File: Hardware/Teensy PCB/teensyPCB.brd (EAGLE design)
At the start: 100 x 50 mm, 0 parts

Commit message: added some parts
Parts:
- added J_BT_BOARD_1: BLUETOOTH_BOARD, Bluetooth_HC-05:BT_BOARD_FOOTPRINT
- added J_ULTRASONIC_1: HC-SR04, HC-SR04:HC-SR04_FOOTPRINT
- added U$1: TEENSY_3.1_ALL_PINS_AND_PADS, Teensy_3_and_LC_Series_Boards_v1.1:TEENSY3_ALL_PINS_&_PADS
- added U1: HC_05, Bluetooth_HC-05:BLUETOOTH_SMD
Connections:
- new net 3.3V: U$1.3.3V, U$1.3.3V1, U$1.3.3V2
- new net AGND: U$1.AGND
- new net AREF: U$1.AREF
- new net GND: U$1.GND, U$1.GND1, U$1.GND2
- new net VBAT: U$1.VBAT
- new net VIN: U$1.VIN
- new net VUSB: U$1.VUSB
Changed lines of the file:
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@@
 <setting verticaltext="up"/>
 </settings>
-<grid distance="50" unitdist="mm" unit="mm" style="lines" multiple="1" display="yes" altdistance="0.025" altunitdist="inch" altunit="inch"/>
+<grid distance="5" unitdist="mm" unit="mm" style="lines" multiple="1" display="yes" altdistance="0.025" altunitdist="inch" altunit="inch"/>
 <layers>
 <layer number="1" name="Top" color="4" fill="1" visible="yes" active="yes"/>
@@
 <layer number="48" name="Document" color="7" fill="1" visible="yes" active="yes"/>
 <layer number="49" name="Reference" color="7" fill="1" visible="yes" active="yes"/>
+<layer number="50" name="dxf" color="7" fill="1" visible="yes" active="yes"/>
 <layer number="51" name="tDocu" color="7" fill="1" visible="yes" active="yes"/>
 <layer number="52" name="bDocu" color="7" fill="1" visible="yes" active="yes"/>
+<layer number="53" name="tGND_GNDA" color="7" fill="9" visible="no" active="no"/>
+<layer number="54" name="bGND_GNDA" color="1" fill="9" visible="no" active="no"/>
+<layer number="56" name="wert" color="7" fill="1" visible="yes" active="yes"/>
 <layer number="90" name="Modules" color="5" fill="1" visible="no" active="no"/>
 <layer number="91" name="Nets" color="2" fill="1" visible="no" active="no"/>
@@
 <layer number="97" name="Info" color="7" fill="1" visible="no" active="no"/>
 <layer number="98" name="Guide" color="6" fill="1" visible="no" active="no"/>
+<layer number="100" name="Muster" color="7" fill="1" visible="no" active="no"/>
+<layer number="101" name="Patch_Top" color="12" fill="4" visible="yes" active="yes"/>
+<layer number="102" name="Vscore" color="7" fill="1" visible="yes" active="yes"/>
+<layer number="104" name="Name" color="7" fill="1" visible="yes" active="yes"/>
+<layer number="116" name="Patch_BOT" color="9" fill="4" visible="yes" active="yes"/>
+<layer number="121" name="_tsilk" color="7" fill="1" visible="yes" active="yes"/>
+<layer number="122" name="_bsilk" color="7" fill="1" visible="yes" active="yes"/>
+<layer number="151" name="HeatSink" color="7" fill="1" visible="yes" active="yes"/>
+<layer number="200" name="200bmp" color="1" fill="10" visible="no" active="no"/>
+<layer number="201" name="201bmp" color="2" fill="1" visible="no" active="no"/>
+<layer number="202" name="202bmp" color="3" fill="1" visible="no" active="no"/>
+<layer number="250" name="Descript" color="3" fill="1" visible="no" active="no"/>
+<layer number="251" name="SMDround" color="12" fill="11" visible="no" active="no"/>
+<layer number="254" name="cooling" color="7" fill="1" visible="yes" active="yes"/>
 </layers>
 <board>
@@
 </autorouter>
 <elements>
+<element name="U$1" library="Teensy_3_and_LC_Series_Boards_v1.1" package="TEENSY3_ALL_PINS_&amp;_PADS" value="TEENSY_3.1_ALL_PINS_AND_PADS" x="-50" y="50"/>
+<element name="U1" library="Bluetooth_HC-05" package="BLUETOOTH_SMD" value="HC_05" x="-100" y="50"/>
+<element name="J_BT_BOARD_1" library="Bluetooth_HC-05" package="BT_BOARD_FOOTPRINT" value="BLUETOOTH_BOARD" x="-30" y="-25"/>
+<element name="J_ULTRASONIC_1" library="HC-SR04" package="HC-SR04_FOOTPRINT" value="HC-SR04" x="-75" y="-25"/>
 </elements>
 <signals>
+<signal name="GND">
+<contactref element="U$1" pad="GND1"/>
+<contactref element="U$1" pad="GND"/>
+<contactref element="U$1" pad="GND2"/>
+<wire x1="-50" y1="48.73" x2="-50" y2="33.49" width="0" layer="19" extent="1-1"/>
+<wire x1="-57.62" y1="66.51" x2="-50" y2="48.73" width="0" layer="19" extent="1-1"/>
+</signal>
+<signal name="VIN">
+<contactref element="U$1" pad="VIN"/>
+</signal>
+<signal name="AGND">
+<contactref element="U$1" pad="AGND"/>
+</signal>
+<signal name="3.3V">
+<contactref element="U$1" pad="3.3V2"/>
+<contactref element="U$1" pad="3.3V1"/>
+<contactref element="U$1" pad="3.3V"/>
+<wire x1="-47.46" y1="48.73" x2="-42.38" y2="61.43" width="0" layer="19" extent="1-1"/>
+<wire x1="-52.54" y1="33.49" x2="-47.46" y2="48.73" width="0" layer="19" extent="1-1"/>
+</signal>
+<signal name="VBAT">
+<contactref element="U$1" pad="VBAT"/>
+</signal>
+<signal name="AREF">
+<contactref element="U$1" pad="AREF"/>
+</signal>
+<signal name="VUSB">
+<contactref element="U$1" pad="VUSB"/>
+</signal>
 </signals>
 </board>

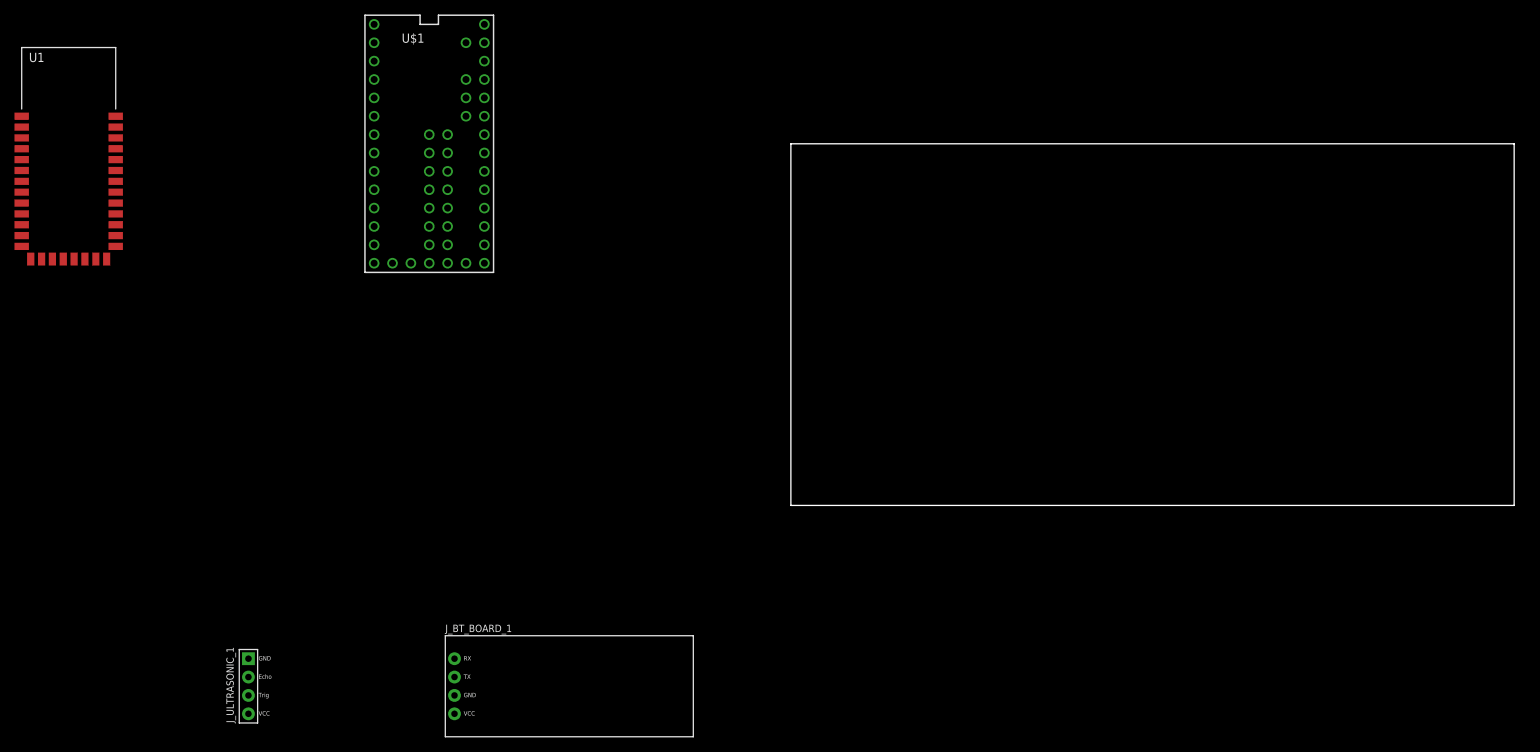
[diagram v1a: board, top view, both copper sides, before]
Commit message: reserving audio pins
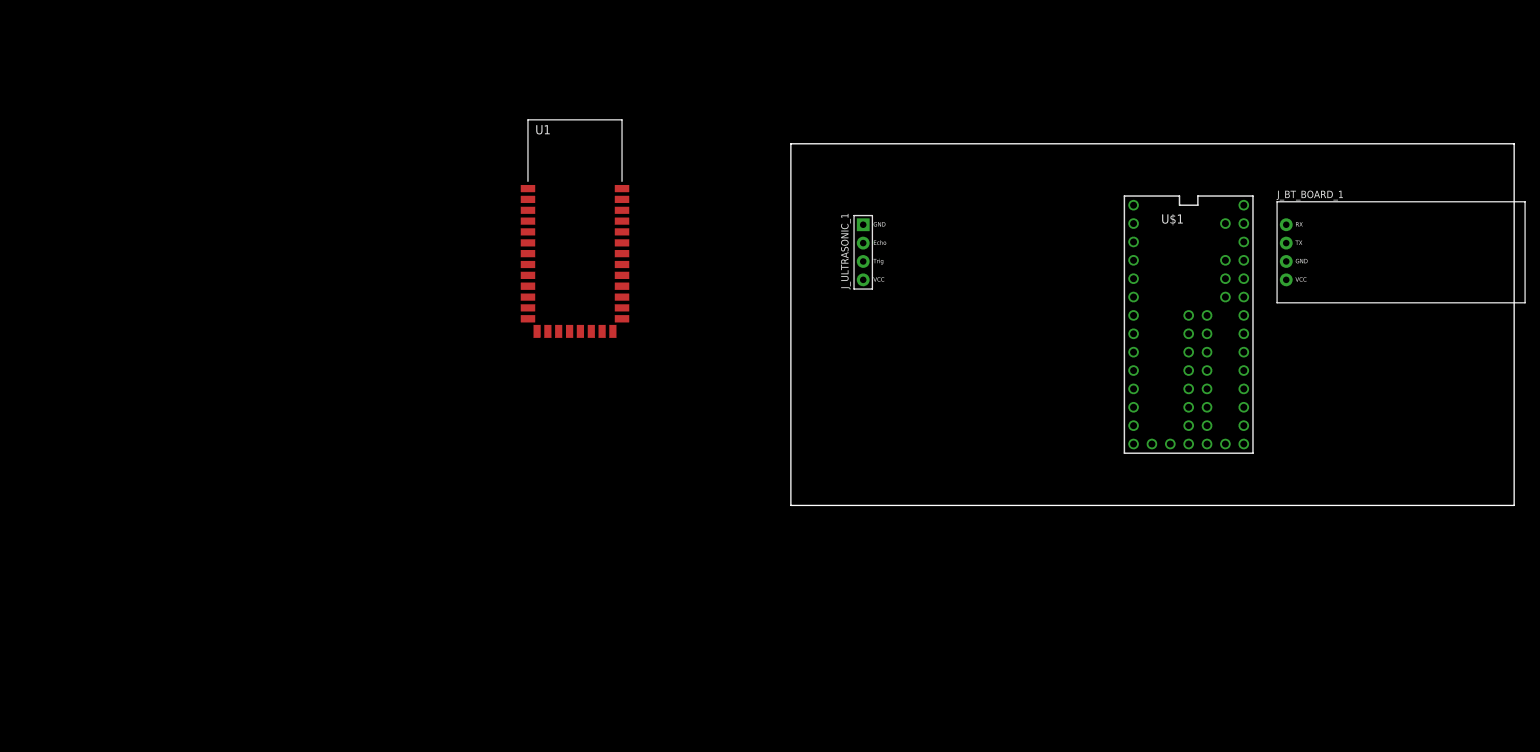
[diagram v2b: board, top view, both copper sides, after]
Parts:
- moved J_BT_BOARD_1 129.7 mm to (85.0, 35.0)
- moved U$1 107.9 mm to (55.0, 25.0)
- moved J_ULTRASONIC_1 104.0 mm to (10.0, 35.0)
- moved U1 70.7 mm to (-30.0, 40.0)
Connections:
- net GND: now also U$1.10, U$1.11, U$1.12, U$1.13, U$1.14/A0, U$1.15/A1, U$1.18/A4, U$1.19/A5, U$1.22/A8, U$1.23/A9, U$1.7, U$1.9
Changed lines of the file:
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@@
 <layer number="101" name="Patch_Top" color="12" fill="4" visible="yes" active="yes"/>
 <layer number="102" name="Vscore" color="7" fill="1" visible="yes" active="yes"/>
+<layer number="103" name="tMap" color="7" fill="1" visible="yes" active="yes"/>
 <layer number="104" name="Name" color="7" fill="1" visible="yes" active="yes"/>
+<layer number="105" name="tPlate" color="7" fill="1" visible="yes" active="yes"/>
+<layer number="106" name="bPlate" color="7" fill="1" visible="yes" active="yes"/>
+<layer number="107" name="Crop" color="7" fill="1" visible="yes" active="yes"/>
+<layer number="108" name="tplace-old" color="10" fill="1" visible="no" active="yes"/>
+<layer number="109" name="ref-old" color="11" fill="1" visible="no" active="yes"/>
 <layer number="116" name="Patch_BOT" color="9" fill="4" visible="yes" active="yes"/>
 <layer number="121" name="_tsilk" color="7" fill="1" visible="yes" active="yes"/>
 <layer number="122" name="_bsilk" color="7" fill="1" visible="yes" active="yes"/>
+<layer number="125" name="_tNames" color="7" fill="1" visible="yes" active="yes"/>
+<layer number="144" name="Drill_legend" color="7" fill="1" visible="yes" active="yes"/>
 <layer number="151" name="HeatSink" color="7" fill="1" visible="yes" active="yes"/>
+<layer number="199" name="Contour" color="7" fill="1" visible="yes" active="yes"/>
 <layer number="200" name="200bmp" color="1" fill="10" visible="no" active="no"/>
 <layer number="201" name="201bmp" color="2" fill="1" visible="no" active="no"/>
 <layer number="202" name="202bmp" color="3" fill="1" visible="no" active="no"/>
+<layer number="203" name="203bmp" color="4" fill="10" visible="yes" active="yes"/>
+<layer number="204" name="204bmp" color="5" fill="10" visible="yes" active="yes"/>
+<layer number="205" name="205bmp" color="6" fill="10" visible="yes" active="yes"/>
+<layer number="206" name="206bmp" color="7" fill="10" visible="yes" active="yes"/>
+<layer number="207" name="207bmp" color="8" fill="10" visible="yes" active="yes"/>
+<layer number="208" name="208bmp" color="9" fill="10" visible="yes" active="yes"/>
+<layer number="209" name="209bmp" color="7" fill="1" visible="yes" active="yes"/>
+<layer number="210" name="210bmp" color="7" fill="1" visible="yes" active="yes"/>
+<layer number="211" name="211bmp" color="7" fill="1" visible="yes" active="yes"/>
+<layer number="212" name="212bmp" color="7" fill="1" visible="yes" active="yes"/>
+<layer number="213" name="213bmp" color="7" fill="1" visible="yes" active="yes"/>
+<layer number="214" name="214bmp" color="7" fill="1" visible="yes" active="yes"/>
+<layer number="215" name="215bmp" color="7" fill="1" visible="yes" active="yes"/>
+<layer number="216" name="216bmp" color="7" fill="1" visible="yes" active="yes"/>
+<layer number="217" name="217bmp" color="18" fill="1" visible="no" active="no"/>
+<layer number="218" name="218bmp" color="19" fill="1" visible="no" active="no"/>
+<layer number="219" name="219bmp" color="20" fill="1" visible="no" active="no"/>
+<layer number="220" name="220bmp" color="21" fill="1" visible="no" active="no"/>
+<layer number="221" name="221bmp" color="22" fill="1" visible="no" active="no"/>
+<layer number="222" name="222bmp" color="23" fill="1" visible="no" active="no"/>
+<layer number="223" name="223bmp" color="24" fill="1" visible="no" active="no"/>
+<layer number="224" name="224bmp" color="25" fill="1" visible="no" active="no"/>
 <layer number="250" name="Descript" color="3" fill="1" visible="no" active="no"/>
 <layer number="251" name="SMDround" color="12" fill="11" visible="no" active="no"/>
@@
 </autorouter>
 <elements>
-<element name="U$1" library="Teensy_3_and_LC_Series_Boards_v1.1" package="TEENSY3_ALL_PINS_&amp;_PADS" value="TEENSY_3.1_ALL_PINS_AND_PADS" x="-50" y="50"/>
-<element name="U1" library="Bluetooth_HC-05" package="BLUETOOTH_SMD" value="HC_05" x="-100" y="50"/>
-<element name="J_BT_BOARD_1" library="Bluetooth_HC-05" package="BT_BOARD_FOOTPRINT" value="BLUETOOTH_BOARD" x="-30" y="-25"/>
-<element name="J_ULTRASONIC_1" library="HC-SR04" package="HC-SR04_FOOTPRINT" value="HC-SR04" x="-75" y="-25"/>
+<element name="U$1" library="Teensy_3_and_LC_Series_Boards_v1.1" package="TEENSY3_ALL_PINS_&amp;_PADS" value="TEENSY_3.1_ALL_PINS_AND_PADS" x="55" y="25"/>
+<element name="U1" library="Bluetooth_HC-05" package="BLUETOOTH_SMD" value="HC_05" x="-30" y="40"/>
+<element name="J_BT_BOARD_1" library="Bluetooth_HC-05" package="BT_BOARD_FOOTPRINT" value="BLUETOOTH_BOARD" x="85" y="35"/>
+<element name="J_ULTRASONIC_1" library="HC-SR04" package="HC-SR04_FOOTPRINT" value="HC-SR04" x="10" y="35"/>
 </elements>
 <signals>
@@
 <contactref element="U$1" pad="GND"/>
 <contactref element="U$1" pad="GND2"/>
-<wire x1="-50" y1="48.73" x2="-50" y2="33.49" width="0" layer="19" extent="1-1"/>
-<wire x1="-57.62" y1="66.51" x2="-50" y2="48.73" width="0" layer="19" extent="1-1"/>
+<contactref element="U$1" pad="18/A4"/>
+<contactref element="U$1" pad="19/A5"/>
+<contactref element="U$1" pad="11"/>
+<contactref element="U$1" pad="9"/>
+<contactref element="U$1" pad="23/A9"/>
+<contactref element="U$1" pad="22/A8"/>
+<contactref element="U$1" pad="13"/>
+<contactref element="U$1" pad="15/A1"/>
+<contactref element="U$1" pad="12"/>
+<contactref element="U$1" pad="14/A0"/>
+<contactref element="U$1" pad="7"/>
+<contactref element="U$1" pad="10"/>
+<wire x1="62.62" y1="31.35" x2="62.62" y2="33.89" width="0" layer="19" extent="1-1"/>
+<wire x1="62.62" y1="23.73" x2="62.62" y2="31.35" width="0" layer="19" extent="1-1"/>
+<wire x1="62.62" y1="21.19" x2="62.62" y2="23.73" width="0" layer="19" extent="1-1"/>
+<wire x1="55" y1="23.73" x2="62.62" y2="23.73" width="0" layer="19" extent="1-1"/>
+<wire x1="62.62" y1="13.57" x2="62.62" y2="21.19" width="0" layer="19" extent="1-1"/>
+<wire x1="62.62" y1="11.03" x2="62.62" y2="13.57" width="0" layer="19" extent="1-1"/>
+<wire x1="62.62" y1="8.49" x2="62.62" y2="11.03" width="0" layer="19" extent="1-1"/>
+<wire x1="55" y1="8.49" x2="62.62" y2="8.49" width="0" layer="19" extent="1-1"/>
+<wire x1="47.38" y1="8.49" x2="55" y2="8.49" width="0" layer="19" extent="1-1"/>
+<wire x1="47.38" y1="11.03" x2="47.38" y2="8.49" width="0" layer="19" extent="1-1"/>
+<wire x1="47.38" y1="13.57" x2="47.38" y2="11.03" width="0" layer="19" extent="1-1"/>
+<wire x1="47.38" y1="16.11" x2="47.38" y2="13.57" width="0" layer="19" extent="1-1"/>
+<wire x1="47.38" y1="21.19" x2="47.38" y2="16.11" width="0" layer="19" extent="1-1"/>
+<wire x1="47.38" y1="41.51" x2="62.62" y2="33.89" width="0" layer="19" extent="1-1"/>
 </signal>
 <signal name="VIN">
@@
 <contactref element="U$1" pad="3.3V1"/>
 <contactref element="U$1" pad="3.3V"/>
-<wire x1="-47.46" y1="48.73" x2="-42.38" y2="61.43" width="0" layer="19" extent="1-1"/>
-<wire x1="-52.54" y1="33.49" x2="-47.46" y2="48.73" width="0" layer="19" extent="1-1"/>
+<wire x1="57.54" y1="23.73" x2="62.62" y2="36.43" width="0" layer="19" extent="1-1"/>
+<wire x1="52.46" y1="8.49" x2="57.54" y2="23.73" width="0" layer="19" extent="1-1"/>
 </signal>
 <signal name="VBAT">
